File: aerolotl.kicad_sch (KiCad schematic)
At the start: 0 parts

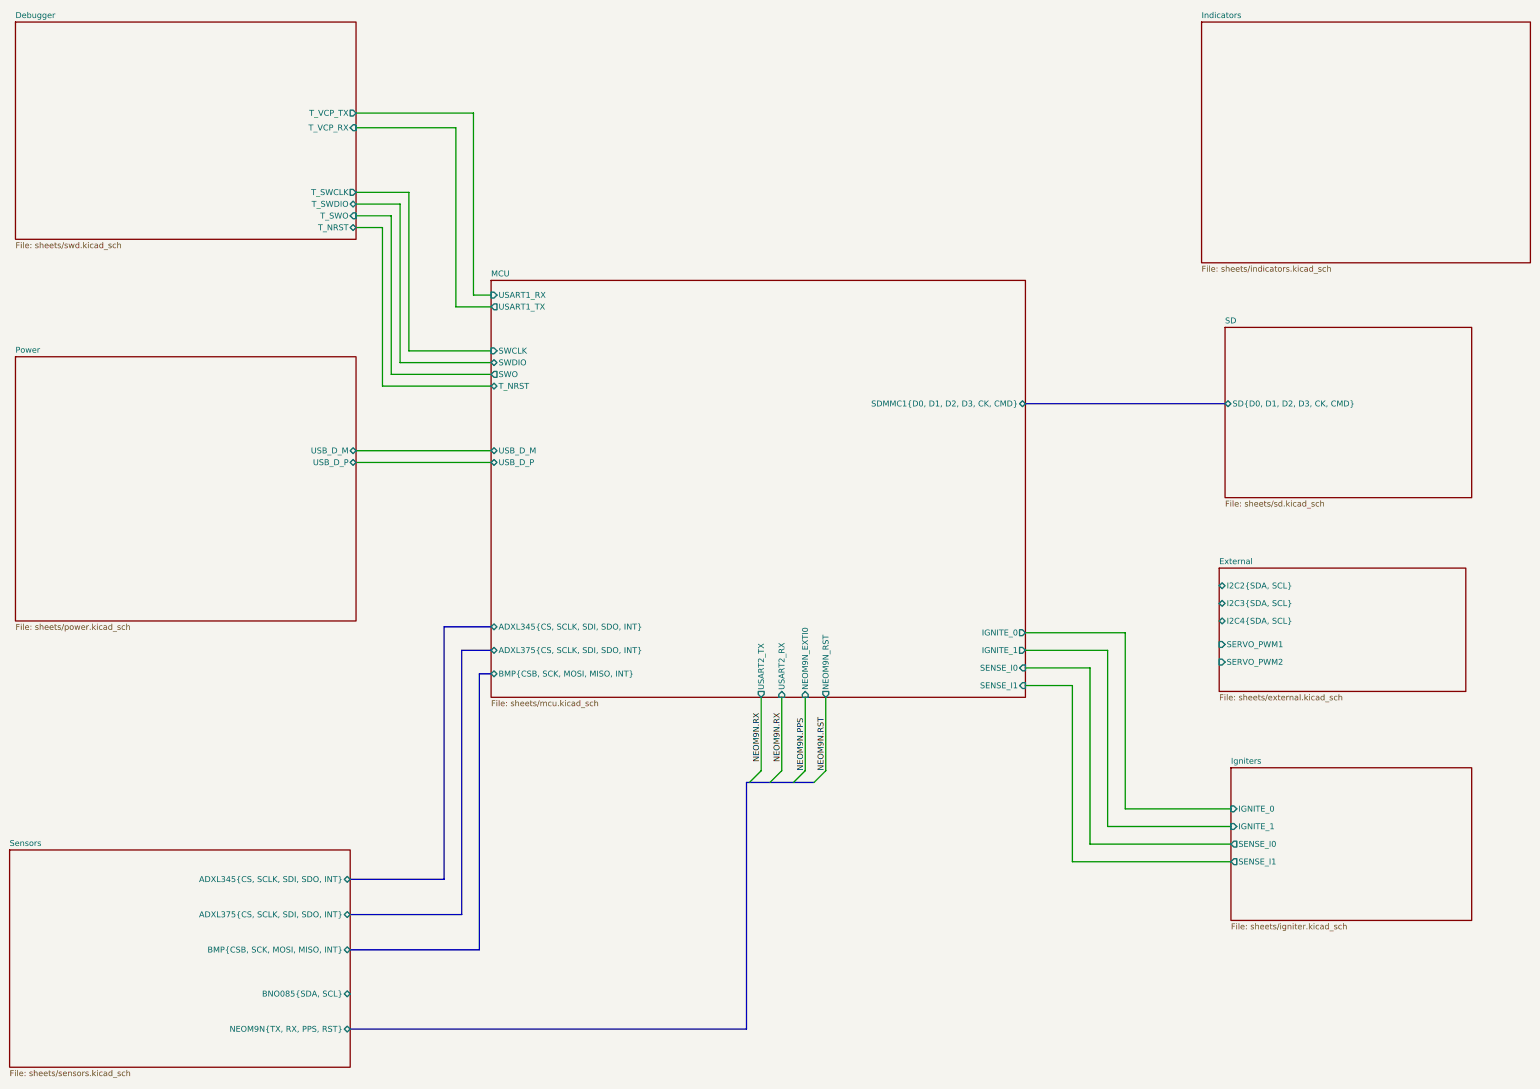
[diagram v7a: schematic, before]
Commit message: removed fd can
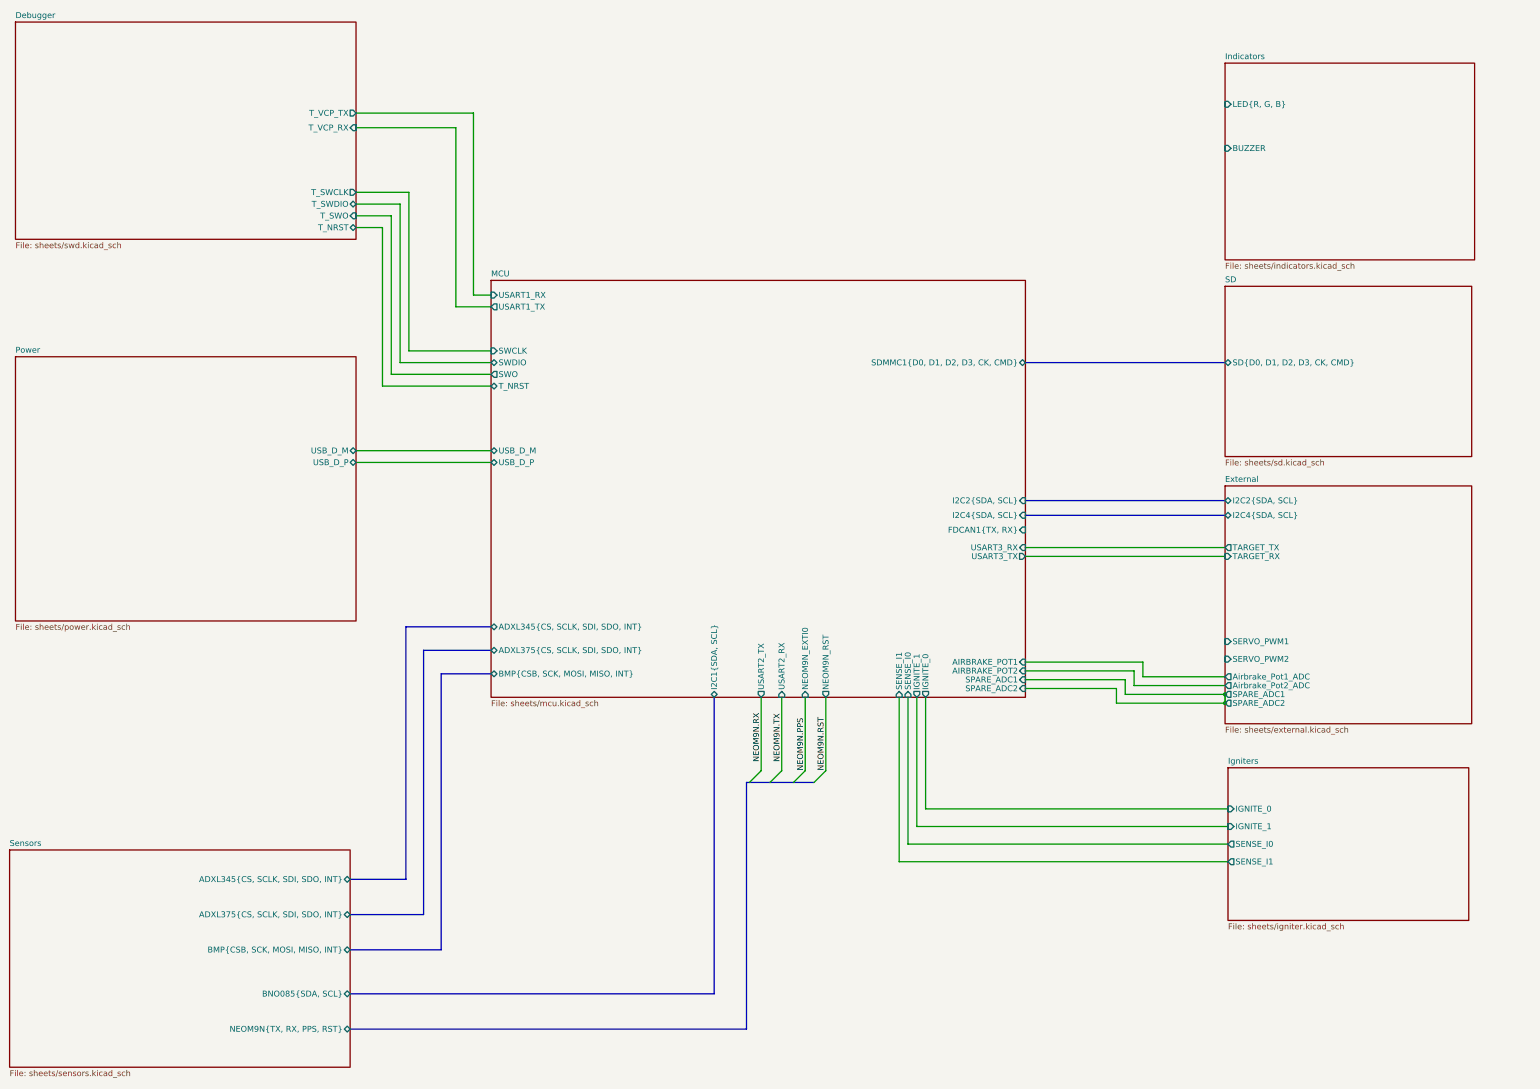
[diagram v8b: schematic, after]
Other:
- sheet External ports: added Airbrake_Pot1_ADC, Airbrake_Pot2_ADC, SPARE_ADC1, SPARE_ADC2, TARGET_RX, TARGET_TX; removed I2C3{SDA, SCL}
- sheet Indicators ports: added BUZZER, LED{R, G, B}; removed none
- sheet MCU ports: added AIRBRAKE_POT1, AIRBRAKE_POT2, FDCAN1{TX, RX}, I2C1{SDA, SCL}, I2C2{SDA, SCL}, I2C4{SDA, SCL}, SPARE_ADC1, SPARE_ADC2, USART3_RX, USART3_TX; removed none
